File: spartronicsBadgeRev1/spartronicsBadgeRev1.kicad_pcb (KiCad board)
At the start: 2 copper layers, 87.6 x 87.5 mm, 54 parts, among them U1 ATmega328PB-AU

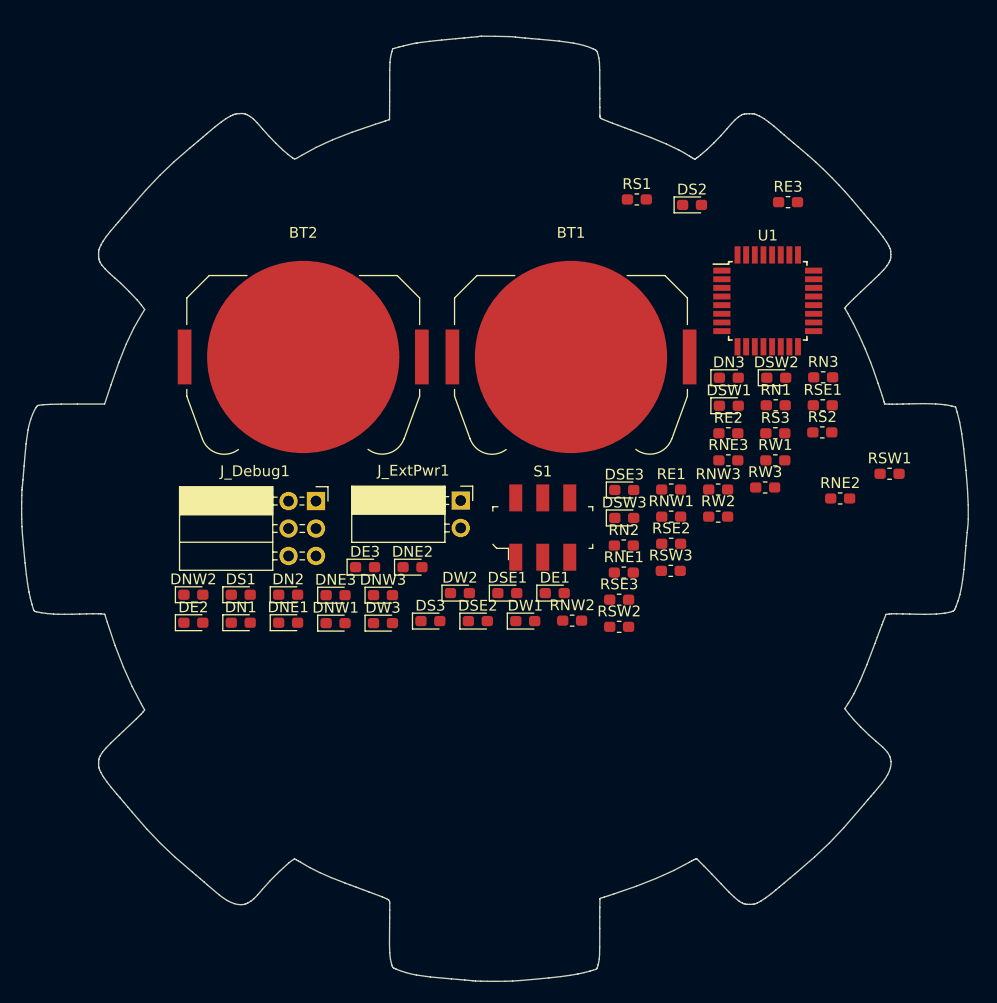
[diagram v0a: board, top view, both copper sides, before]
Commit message: Moved all the LED's to the teeth. Some silkscreen still has to be moved, need to change CON footprint + label it
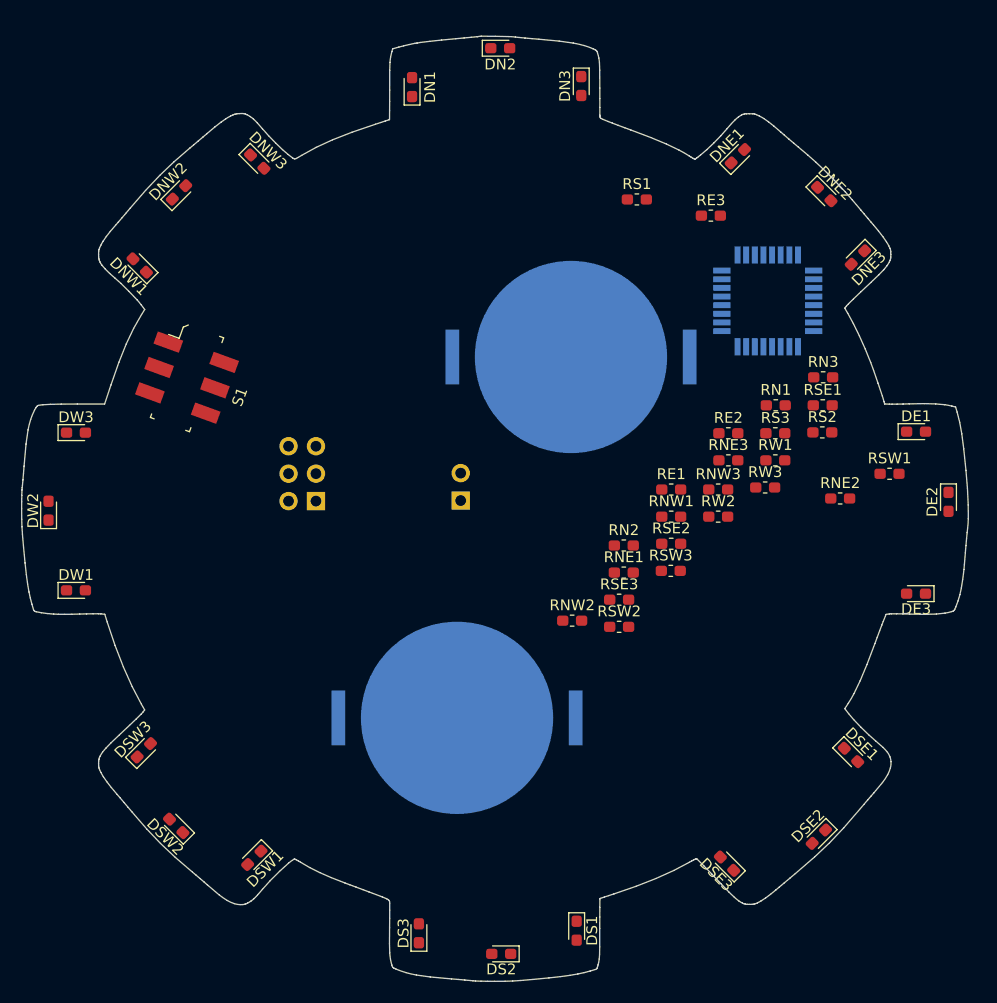
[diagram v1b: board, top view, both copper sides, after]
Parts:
- BT1, BT2, J_Debug1, J_ExtPwr1, U1: moved to B.Cu
- moved DS2 71.6 mm to (148.6, 133.3), turned to 180 degrees
- moved DE2 70.8 mm to (190.0, 91.5), turned to 270 degrees
- moved DSW2 69.3 mm to (118.5, 121.5), turned to 135 degrees
- moved DSW1 60.7 mm to (125.7, 124.5), turned to 225 degrees
- moved DNE1 60.0 mm to (170.5, 59.5), turned to 45 degrees
- moved DNE3 57.6 mm to (181.6, 68.9), turned to 225 degrees
- moved DN2 54.3 mm to (148.5, 49.5)
- moved DN1 52.1 mm to (140.3, 53.1), turned to 90 degrees
- moved DNE2 51.5 mm to (178.5, 63.0), turned to 315 degrees
- moved DE3 51.1 mm to (187.0, 100.0), turned to 180 degrees
- moved DSW3 49.4 mm to (115.5, 114.5), turned to 45 degrees
- moved DS1 44.0 mm to (155.6, 131.2), turned to 270 degrees
- moved DNW3 41.8 mm to (126.0, 60.0), turned to 315 degrees
- moved DW1 41.7 mm to (109.2, 99.7)
- moved DW2 38.8 mm to (106.7, 92.3), turned to 90 degrees
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
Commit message: Checkpoint before doing routing, in case of error
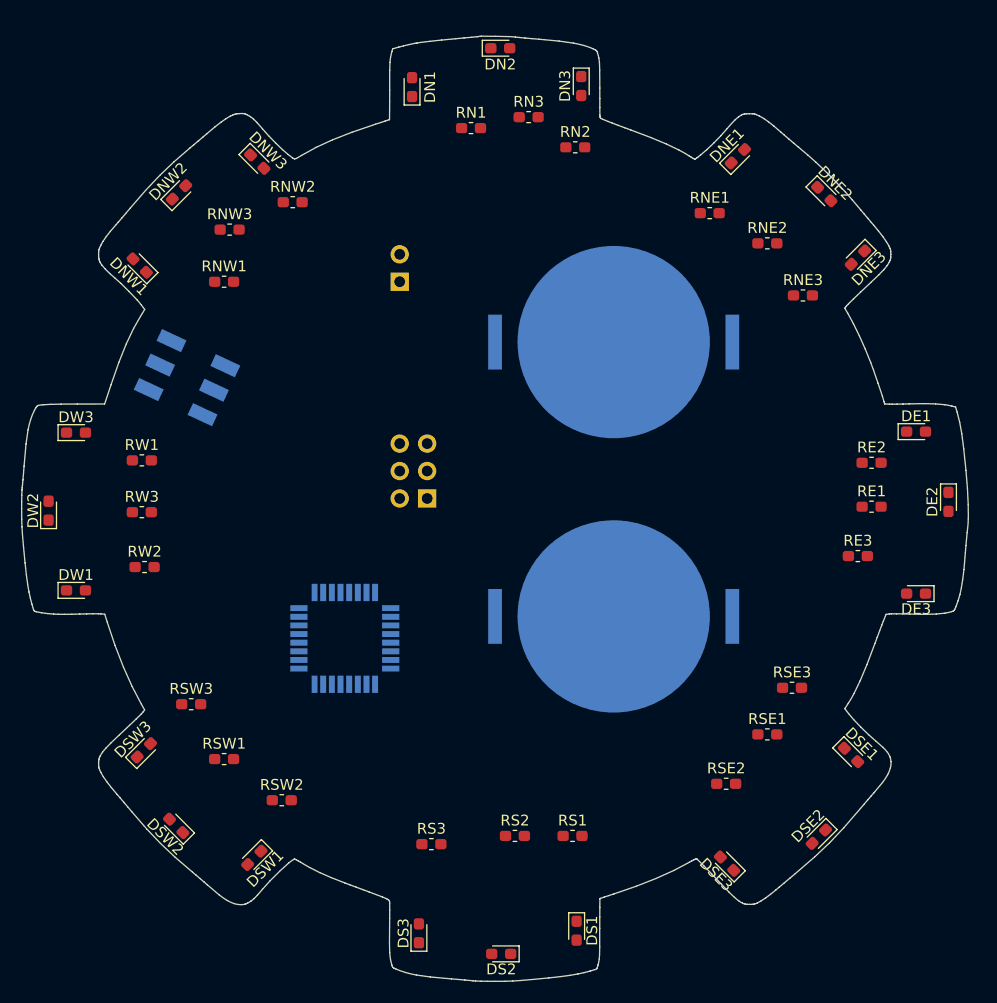
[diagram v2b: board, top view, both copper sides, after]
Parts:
- added ?: , , F.Cu at (131.6, 95.2)
- S1: moved to B.Cu
- moved RSW1 67.0 mm to (122.9, 115.3)
- moved RS1 59.2 mm to (155.2, 122.4)
- moved RW1 58.7 mm to (115.3, 87.7)
- moved RW3 57.8 mm to (115.3, 92.5)
- moved RW2 53.3 mm to (115.6, 97.5)
- moved RNW3 51.2 mm to (123.4, 66.3)
- moved U1 50.1 mm to (134.1, 104.1), turned to 180 degrees
- moved RS3 49.6 mm to (142.1, 123.2)
- moved RS2 47.0 mm to (149.9, 122.4)
- moved RNW1 46.8 mm to (122.9, 71.1)
- moved RNW2 46.6 mm to (129.3, 63.8)
- moved RSW3 46.1 mm to (119.9, 110.2)
- moved RN1 38.1 mm to (145.8, 56.9)
- moved RN2 37.1 mm to (155.4, 58.7)
- moved RN3 36.4 mm to (151.1, 55.9)
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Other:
- board text added: "BAT VCC"
- board text added: "GND"
- board text added: "MISO"
- board text added: "MOSI"
- board text added: "RESET"
- board text added: "SCK0"
- board text added: "VCC"

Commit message: Finished routing, labels on back, added ground plane. Almost ready for build
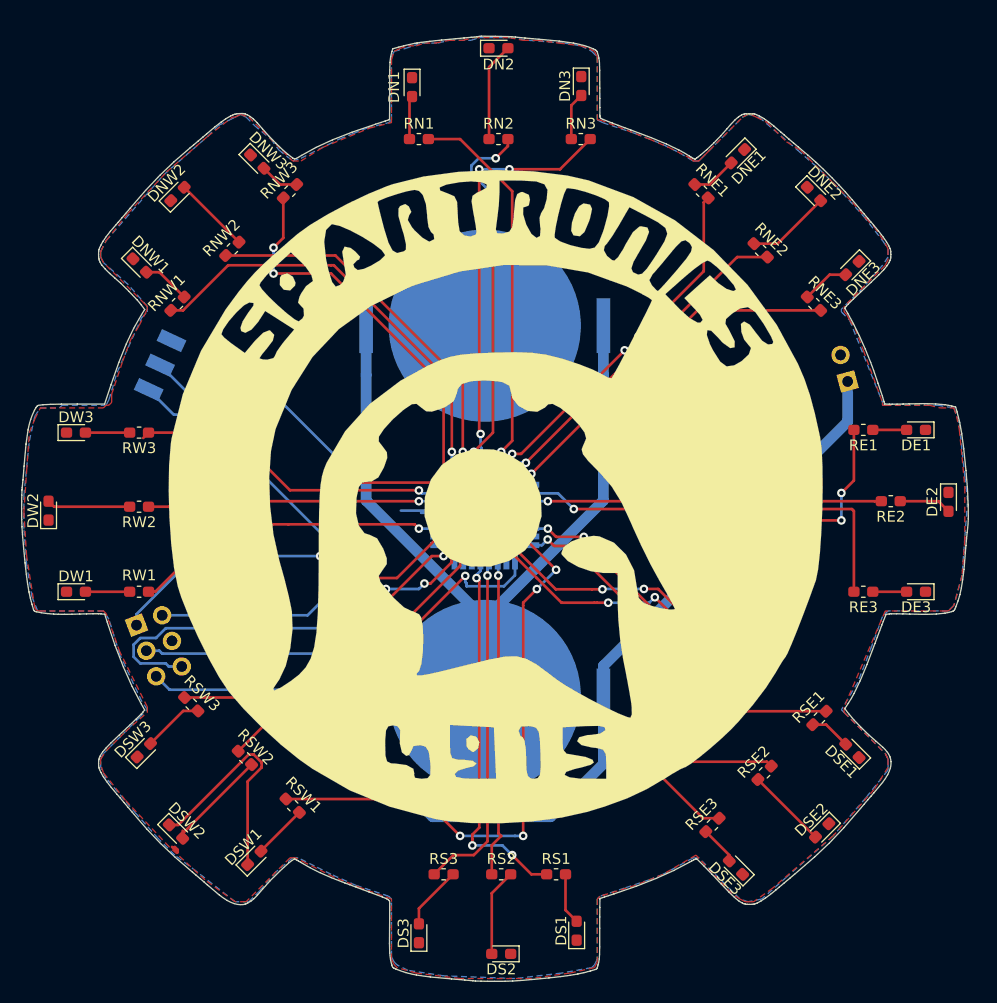
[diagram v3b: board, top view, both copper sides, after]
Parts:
- added G***: LOGO, logoLib:spartronicsNoBorder, F.Cu at (148.1, 90.7)
- moved J_ExtPwr1 42.5 mm to (180.7, 80.4), turned to 15 degrees
- moved BT1 34.9 mm to (147.1, 109.5)
- moved BT2 29.5 mm to (147.1, 75.2)
- moved J_Debug1 29.4 mm to (114.8, 102.9), turned to 201 degrees
- moved U1 17.3 mm to (147.1, 92.7)
- moved RSE3 14.7 mm to (168.1, 121.4), turned to 45 degrees
- moved RW1 12.2 mm to (115.1, 99.8), turned to 180 degrees
- moved RSW1 7.68 mm to (129.3, 119.6), turned to 315 degrees
- moved RW3 7.37 mm to (115.1, 85.1), turned to 180 degrees
- moved RE1 7.15 mm to (182.1, 84.8), turned to 180 degrees
- moved RN2 7.15 mm to (148.3, 57.9)
- moved RNW2 7.06 mm to (123.7, 68.1), turned to 45 degrees
- moved RNW3 6.62 mm to (129.0, 62.7), turned to 45 degrees
- moved RW2 5.61 mm to (115.1, 91.9), turned to 180 degrees
- moved RN3 5.24 mm to (156.0, 57.9)
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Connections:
- J_Debug1 pad 5: NWLED1_SIG -> SCK0
- RSW2 pad 1: SWLED2_SIG -> SCK0
- U1 pad 1: SLED1_SIG -> NELED1_SIG
- U1 pad 10: WLED1_SIG -> ELED1_SIG
- U1 pad 11: WLED2_SIG -> SLED2_SIG
- U1 pad 12: NLED1_SIG -> SLED3_SIG
- U1 pad 13: NLED2_SIG -> SLED1_SIG
- U1 pad 14: NLED3_SIG -> SELED1_SIG
- U1 pad 17: NWLED1_SIG -> SCK0
- U1 pad 19: SWLED1_SIG -> WLED2_SIG
- U1 pad 2: SLED2_SIG -> ELED3_SIG
- U1 pad 22: WLED3_SIG -> WLED1_SIG
- U1 pad 23: NELED1_SIG -> WLED3_SIG
- U1 pad 24: NELED2_SIG -> NWLED3_SIG
- U1 pad 25: NELED3_SIG -> NWLED1_SIG
- U1 pad 26: ELED1_SIG -> NWLED2_SIG
- U1 pad 27: ELED2_SIG -> NLED2_SIG
- U1 pad 28: ELED3_SIG -> NLED1_SIG
- U1 pad 3: SWLED3_SIG -> ELED2_SIG
- U1 pad 30: SELED1_SIG -> NLED3_SIG
- U1 pad 31: SELED2_SIG -> NELED3_SIG
- U1 pad 32: SELED3_SIG -> NELED2_SIG
- U1 pad 6: SWLED2_SIG -> SELED3_SIG
- U1 pad 7: NWLED2_SIG -> SWLED1_SIG
- U1 pad 8: NWLED3_SIG -> SELED2_SIG
- U1 pad 9: SLED3_SIG -> SWLED3_SIG
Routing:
- net BAT_VCC: track 0.00 -> 114.6 mm
- net Net-(BT1-Pad2): track 0.00 -> 72.6 mm
- net VCC: track 0.00 -> 70.3 mm, vias 0 -> 4
- net SWLED1_SIG: track 0.00 -> 55.7 mm, vias 0 -> 5
- net ELED1_SIG: track 0.00 -> 49.4 mm, vias 0 -> 5
- net SELED1_SIG: track 0.00 -> 46.5 mm, vias 0 -> 3
- net GND: track 0.00 -> 45.7 mm
- net MISO0: track 0.00 -> 44.4 mm, vias 0 -> 4
- net SCK0: track 0.00 -> 41.5 mm, vias 0 -> 3
- net NWLED1_SIG: track 0.00 -> 40.3 mm, vias 0 -> 1
- net NLED1_SIG: track 0.00 -> 39.3 mm, vias 0 -> 3
- net SELED3_SIG: track 0.00 -> 38.5 mm, vias 0 -> 3
- net SELED2_SIG: track 0.00 -> 38.1 mm, vias 0 -> 1
- net ELED3_SIG: track 0.00 -> 38.1 mm, vias 0 -> 1
- net SWLED3_SIG: track 0.00 -> 37.9 mm, vias 0 -> 1
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- added copper zone on B.Cu, net GND
- added copper zone on F.Cu, net GND
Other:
- board text added: "EXT VCC"
- board text added: "East"
- board text added: "North"
- board text added: "Note: If using external power, remove all coin cells"
- board text added: "OFF"
- board text added: "ON"
- board text added: "South"
- board text added: "Spartronics #4915 Competition Badge Revision I"
- board text added: "West"
- board text removed: "BAT VCC"

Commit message: :dizzy: Re-assigning footprint to Diodes + Debug connector (Had to re-assign some pins) (Full 3D render now!)
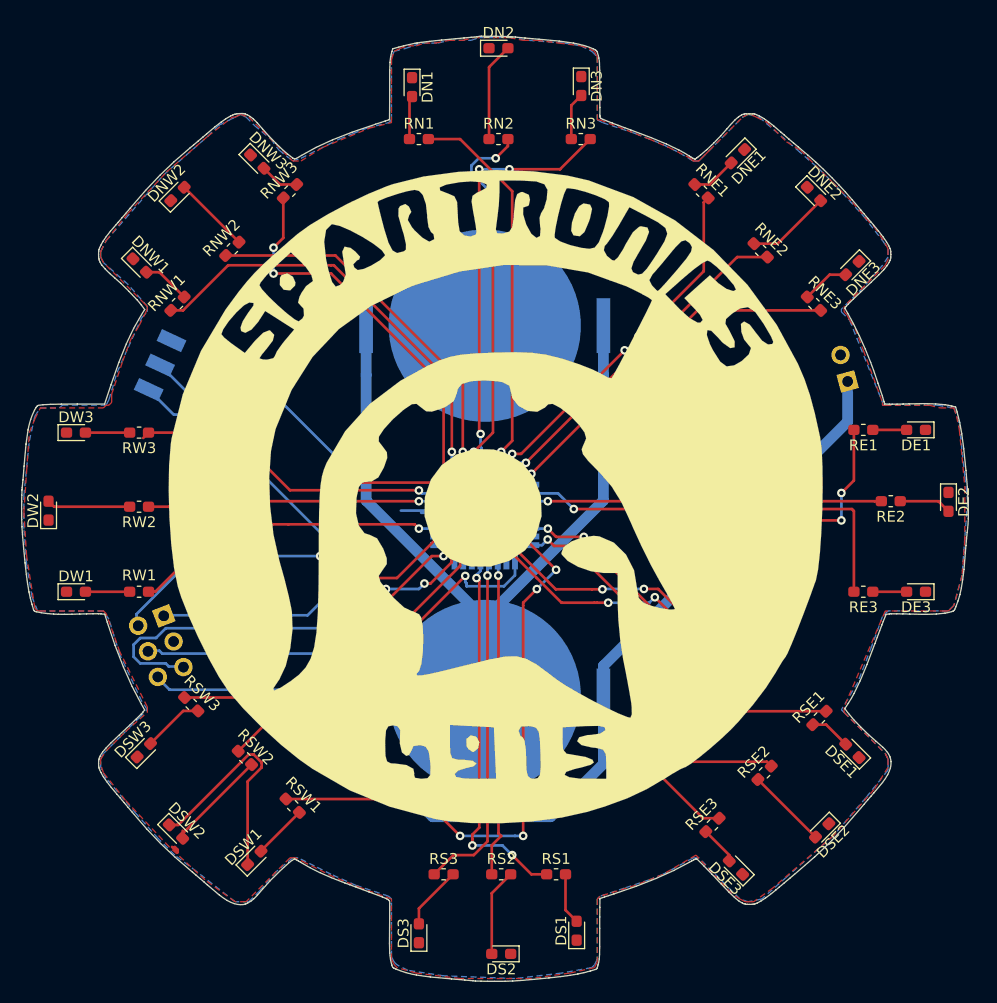
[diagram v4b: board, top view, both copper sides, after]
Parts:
- DE1, DE2, DE3, DN1, DN2, DN3, DNE1, DNE2, DNE3, DNW1, DNW2, DNW3, DS1, DS2, DS3, DSE1, DSE2, DSE3, DSW1, DSW2, DSW3, DW1, DW2, DW3: footprint Diode_SMD:D_0603_1608Metric_Pad1.05x0.95mm_HandSolder -> LED_SMD:LED_0603_1608Metric_Pad1.05x0.95mm_HandSolder
- J_Debug1: footprint Connector_PinSocket_2.54mm:PinSocket_2x03_P2.54mm_Horizontal -> Connector_PinHeader_2.54mm:PinHeader_2x03_P2.54mm_Vertical
- J_ExtPwr1: footprint Connector_PinSocket_2.54mm:PinSocket_1x02_P2.54mm_Horizontal -> Connector_PinHeader_2.54mm:PinHeader_1x02_P2.54mm_Vertical
- moved J_Debug1 2.67 mm to (117.3, 102.1)
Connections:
- J_Debug1 pad 1: VCC -> RESET
- J_Debug1 pad 2: RESET -> VCC
- J_Debug1 pad 3: MOSI0 -> GND
- J_Debug1 pad 4: GND -> MOSI0
